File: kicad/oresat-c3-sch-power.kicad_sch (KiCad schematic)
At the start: 67 parts, among them U31 LP2985AIM5-3.3, U34 TPS259621DDA, U35 TPS259620DDA, U36 LTC3624-5, U38 LP2985AIM5-3.3, U6 LTC3624-5

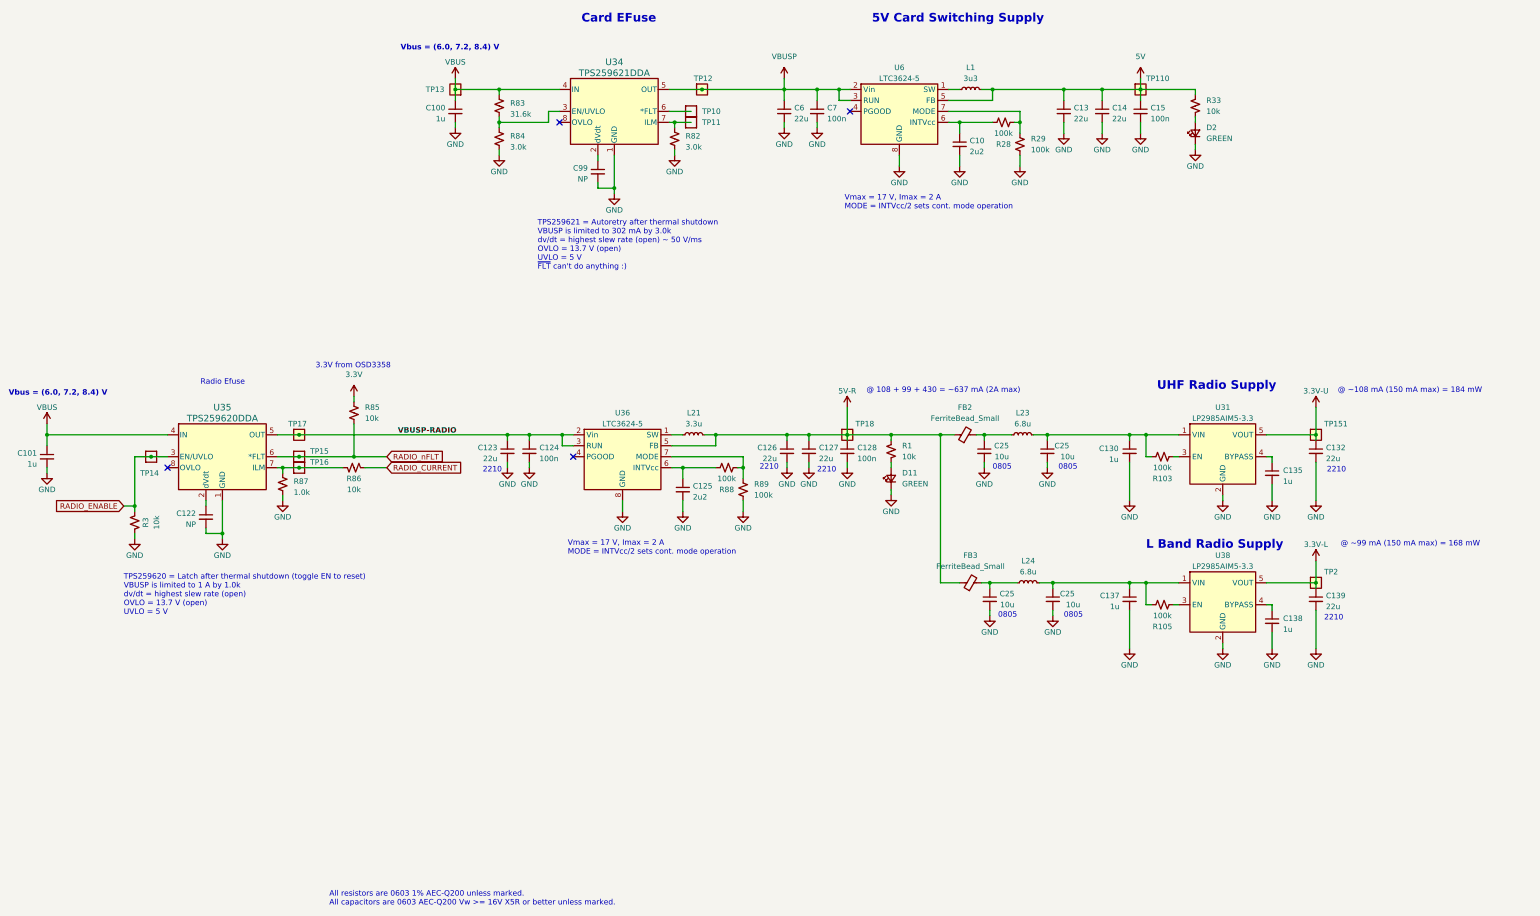
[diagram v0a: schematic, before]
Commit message: More fixes. TOT_CLEAR moved to a non HH pin, cleaned up in2 zones, moved fiducials, set dv/dt on power switches, added HW ID (5 bits) rechecked ADC 1.8V limits and fixed resistor values to match.
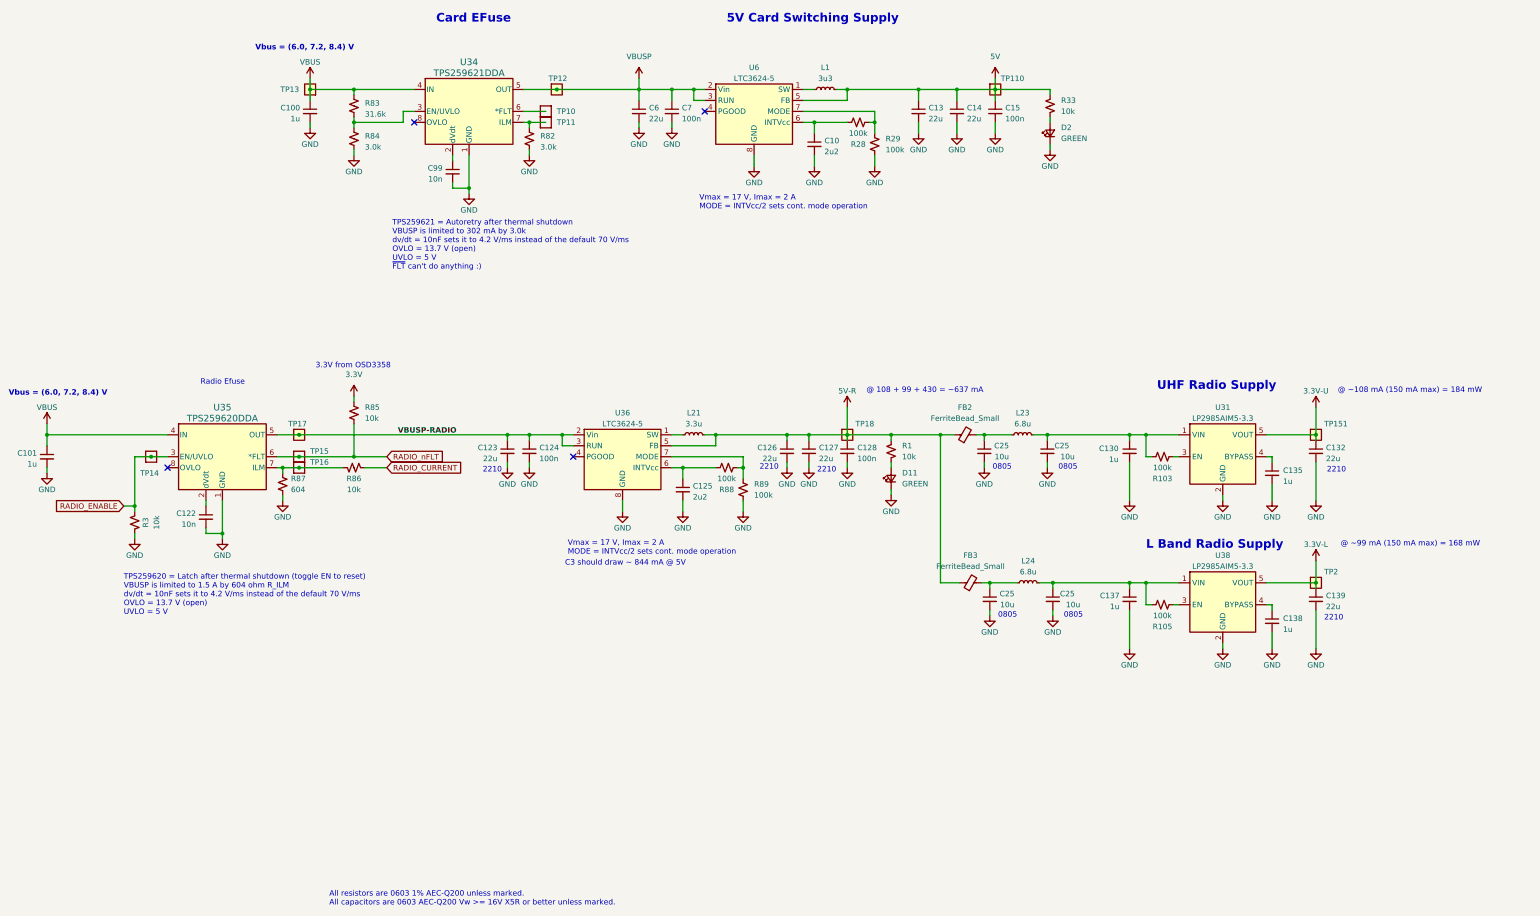
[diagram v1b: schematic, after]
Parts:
- C122, C99: value NP -> 10n
- R87: value 1.0k -> 604
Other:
- note added: "@ 108 + 99 + 430 = ~637 mA"
- note added: "C3 should draw ~ 844 mA @ 5V"
- note added: "TPS259620 = Latch after thermal shutdown (toggle EN to reset) VBUSP is limited to 1.5 A by 604 ohm R_ILM dv/dt = 10nF sets it to 4.2 V/ms instead of the default 70 V/ms OVLO = 13.7 V (open) UVLO = 5 V"
- note added: "TPS259621 = Autoretry after thermal shutdown VBUSP is limited to 302 mA by 3.0k dv/dt = 10nF sets it to 4.2 V/ms instead of the default 70 V/ms OVLO = 13.7 V (open) UVLO = 5 V ~{FLT} can't do anything :)"
- note removed: "@ 108 + 99 + 430 = ~637 mA (2A max)"
- note removed: "TPS259620 = Latch after thermal shutdown (toggle EN to reset) VBUSP is limited to 1 A by 1.0k dv/dt = highest slew rate (open) OVLO = 13.7 V (open) UVLO = 5 V"
- note removed: "TPS259621 = Autoretry after thermal shutdown VBUSP is limited to 302 mA by 3.0k dv/dt = highest slew rate (open) ~ 50 V/ms OVLO = 13.7 V (open) UVLO = 5 V ~{FLT} can't do anything :)"
- moved on the sheet: C10, C100, C13, C14, C15, C6, C7, C99, D2, L1, R28, R29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

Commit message: Ryan made me do it: added CAN0 tranceiver.
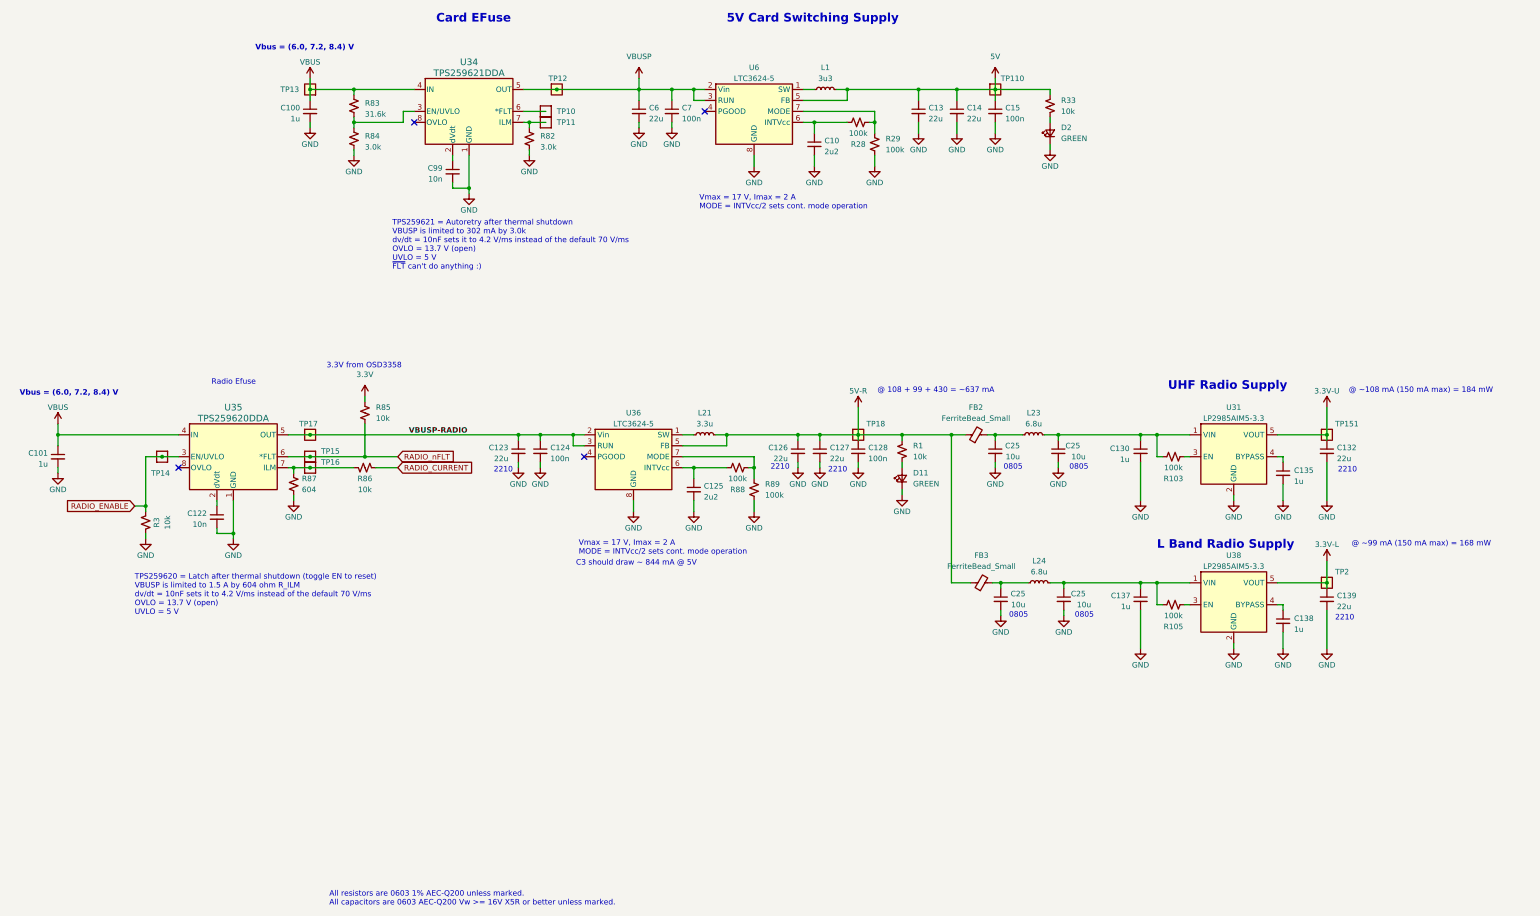
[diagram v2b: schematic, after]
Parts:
- U36, U6: footprint Package_DFN_QFN:DFN-8-1EP_3x3mm_P0.5mm_EP1.65x2.38mm_ThermalVias -> oresat-ics:DFN-8-1EP_3x3mm_P0.5mm_EP1.65x2.38mm_ThermalVias0.3mm
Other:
- moved on the sheet: C101, C122, C123, C124, C125, C126, C127, C128, C130, C132, C135, C137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

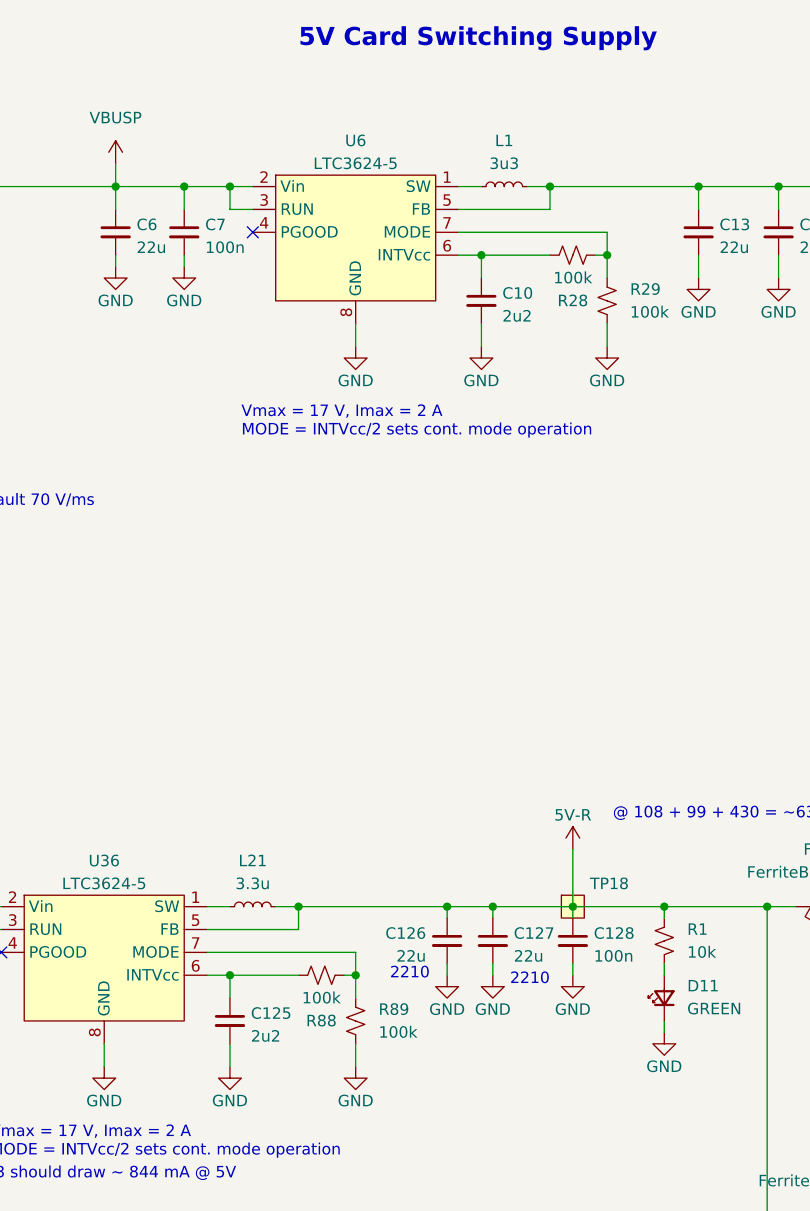
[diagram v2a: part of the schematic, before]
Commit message: First round of BOM fixes and optimizations.
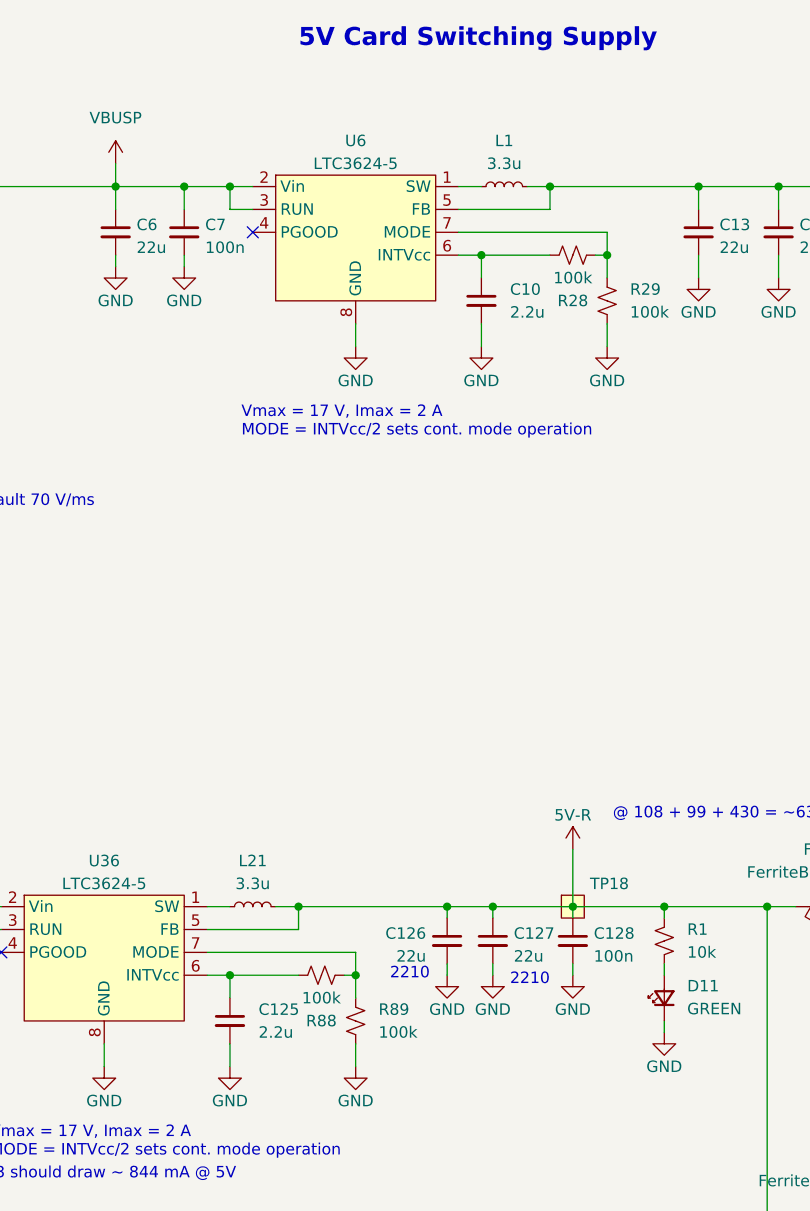
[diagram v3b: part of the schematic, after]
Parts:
- C10, C125: value 2u2 -> 2.2u
- L1: value 3u3 -> 3.3u
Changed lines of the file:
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@@
   (symbol (lib_id "Device:C_Small") (at 202.565 165.1 0) (unit 1)
     (in_bom yes) (on_board yes) (dnp no) (fields_autoplaced)
-    (property "Reference" "C125" (at 204.8891 164.2716 0)
-      (effects (font (size 1.27 1.27)) (justify left))
-    )
-    (property "Value" "2u2" (at 204.8891 166.8085 0)
+    (property "Reference" "C125" (at 205.74 163.8363 0)
+      (effects (font (size 1.27 1.27)) (justify left))
+    )
+    (property "Value" "2.2u" (at 205.74 166.3763 0)
       (effects (font (size 1.27 1.27)) (justify left))
     )
@@
   (symbol (lib_id "Device:C_Small") (at 230.505 85.09 0) (unit 1)
     (in_bom yes) (on_board yes) (dnp no) (fields_autoplaced)
-    (property "Reference" "C10" (at 232.8291 84.2616 0)
-      (effects (font (size 1.27 1.27)) (justify left))
-    )
-    (property "Value" "2u2" (at 232.8291 86.7985 0)
+    (property "Reference" "C10" (at 233.68 83.8263 0)
+      (effects (font (size 1.27 1.27)) (justify left))
+    )
+    (property "Value" "2.2u" (at 233.68 86.3663 0)
       (effects (font (size 1.27 1.27)) (justify left))
     )
@@
       (effects (font (size 1.27 1.27)))
     )
-    (property "Value" "3u3" (at 233.045 69.85 90)
-      (effects (font (size 1.27 1.27)))
-    )
+    (property "Value" "3.3u" (at 233.045 69.85 90)
+      (effects (font (size 1.27 1.27)))
+    )

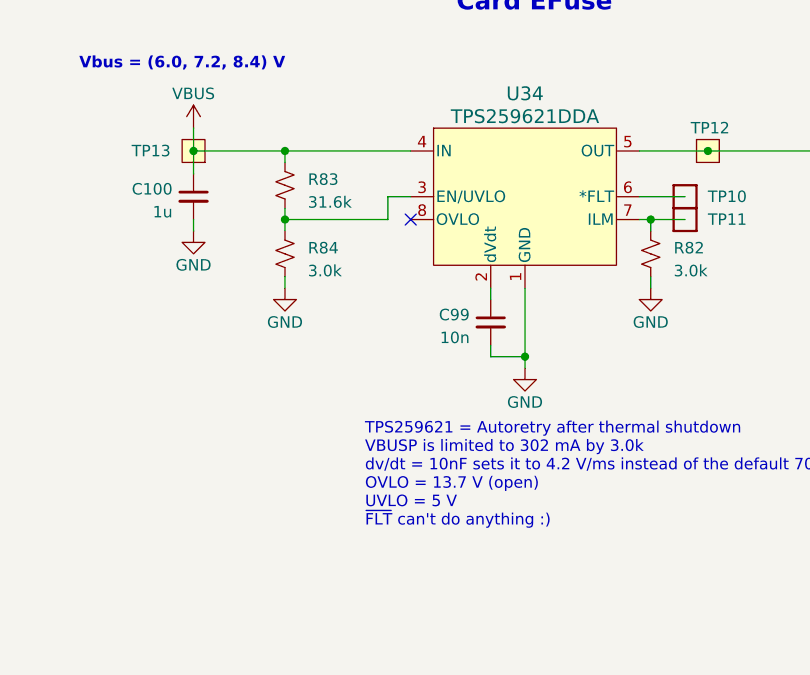
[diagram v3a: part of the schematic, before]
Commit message: More changes to 6.1: fix UVLO on TPS, fix uSD card datasheet link, fix MMC number for SD card
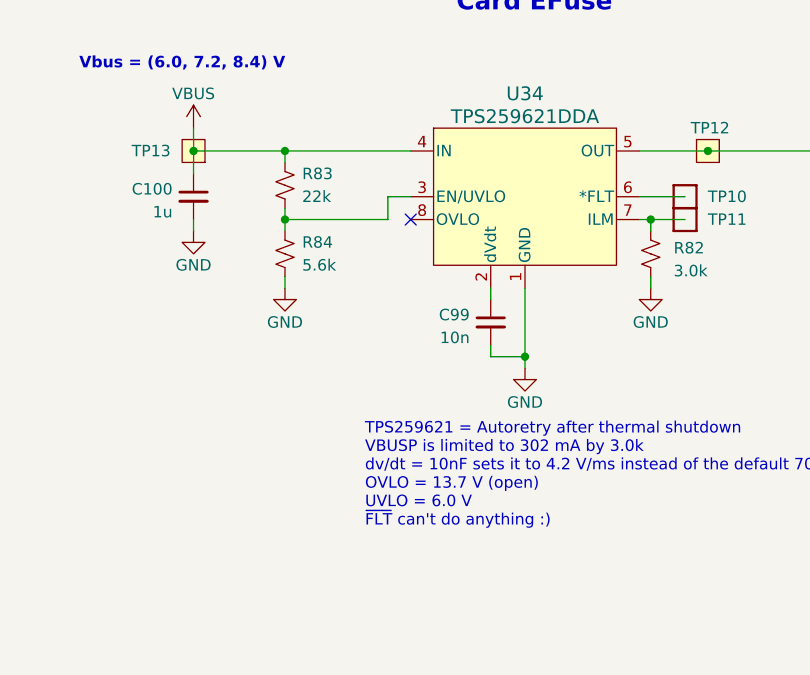
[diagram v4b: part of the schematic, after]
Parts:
- R83: value 31.6k -> 22k
- R84: value 3.0k -> 5.6k
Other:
- note added: "TPS259621 = Autoretry after thermal shutdown VBUSP is limited to 302 mA by 3.0k dv/dt = 10nF sets it to 4.2 V/ms instead of the default 70 V/ms OVLO = 13.7 V (open) UVLO = 6.0 V ~{FLT} can't do anything :)"
- note removed: "TPS259621 = Autoretry after thermal shutdown VBUSP is limited to 302 mA by 3.0k dv/dt = 10nF sets it to 4.2 V/ms instead of the default 70 V/ms OVLO = 13.7 V (open) UVLO = 5 V ~{FLT} can't do anything :)"
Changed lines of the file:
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@@
     (effects (font (size 1.27 1.27)) (justify left bottom))
   )
-  (text "TPS259621 = Autoretry after thermal shutdown\nVBUSP is limited to 302 mA by 3.0k\ndv/dt = 10nF sets it to 4.2 V/ms instead of the default 70 V/ms\nOVLO = 13.7 V (open)\nUVLO = 5 V\n~{FLT} can't do anything :)"
+  (text "TPS259621 = Autoretry after thermal shutdown\nVBUSP is limited to 302 mA by 3.0k\ndv/dt = 10nF sets it to 4.2 V/ms instead of the default 70 V/ms\nOVLO = 13.7 V (open)\nUVLO = 6.0 V\n~{FLT} can't do anything :)"
     (at 132.715 114.3 0)
     (effects (font (size 1.27 1.27)) (justify left bottom))
@@
   (symbol (lib_id "Device:R_Small_US") (at 123.825 76.2 0) (unit 1)
     (in_bom yes) (on_board yes) (dnp no) (fields_autoplaced)
-    (property "Reference" "R83" (at 126.365 75.565 0)
-      (effects (font (size 1.27 1.27)) (justify left))
-    )
-    (property "Value" "31.6k" (at 126.365 78.105 0)
+    (property "Reference" "R83" (at 125.73 74.93 0)
+      (effects (font (size 1.27 1.27)) (justify left))
+    )
+    (property "Value" "22k" (at 125.73 77.47 0)
       (effects (font (size 1.27 1.27)) (justify left))
     )
@@
   (symbol (lib_id "Device:R_Small_US") (at 123.825 83.82 0) (unit 1)
     (in_bom yes) (on_board yes) (dnp no) (fields_autoplaced)
-    (property "Reference" "R84" (at 126.365 83.185 0)
-      (effects (font (size 1.27 1.27)) (justify left))
-    )
-    (property "Value" "3.0k" (at 126.365 85.725 0)
-      (effects (font (size 1.27 1.27)) (justify left))
-    )
+    (property "Reference" "R84" (at 125.73 82.55 0)
+      (effects (font (size 1.27 1.27)) (justify left))
+    )
+    (property "Value" "5.6k" (at 125.73 85.09 0)
+      (effects (font (size 1.27 1.27)) (justify left))
+    )
